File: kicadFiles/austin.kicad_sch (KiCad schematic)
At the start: 482 parts, among them J1 TYPE-C-31-M12_13, J5 Conn_ARM_JTAG_SWD_10, Q1 AO4406AL, SW1 MXSwitch, SW10 MXSwitch, SW100 MXSwitch, SW101 MXSwitch, SW102 MXSwitch, SW103 MXSwitch, SW104 MXSwitch, SW105 MXSwitch, SW106 MXSwitch, SW107 MXSwitch, SW108 MXSwitch, SW109 MXSwitch, SW11 MXSwitch, SW110 MXSwitch, SW111 MXSwitch, SW112 MXSwitch, SW113 MXSwitch, SW114 MXSwitch, SW12 MXSwitch, SW13 MXSwitch, SW14 MXSwitch, SW15 MXSwitch, SW16 MXSwitch, SW17 MXSwitch, SW18 MXSwitch, SW19 MXSwitch, SW2 MXSwitch, SW20 MXSwitch, SW21 MXSwitch, SW22 MXSwitch, SW23 MXSwitch, SW24 MXSwitch, SW25 MXSwitch, SW26 MXSwitch, SW27 MXSwitch, SW28 MXSwitch, SW29 MXSwitch, SW3 MXSwitch, SW30 MXSwitch, SW31 MXSwitch, SW32 MXSwitch, SW33 MXSwitch, SW34 MXSwitch, SW35 MXSwitch, SW36 MXSwitch, SW37 MXSwitch, SW38 MXSwitch, SW39 MXSwitch, SW4 MXSwitch, SW40 MXSwitch, SW41 MXSwitch, SW42 MXSwitch, SW43 MXSwitch, SW44 MXSwitch, SW45 MXSwitch, SW46 MXSwitch, SW47 MXSwitch, SW48 MXSwitch, SW49 MXSwitch, SW5 MXSwitch, SW50 MXSwitch, SW51 MXSwitch, SW52 MXSwitch, SW53 MXSwitch, SW54 MXSwitch, SW55 MXSwitch, SW56 MXSwitch, SW57 MXSwitch, SW58 ANSI LShift, SW59 MXSwitch, SW6 MXSwitch, SW60 MXSwitch, SW61 MXSwitch, SW62 MXSwitch, SW63 MXSwitch, SW64 MXSwitch, SW65 MXSwitch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

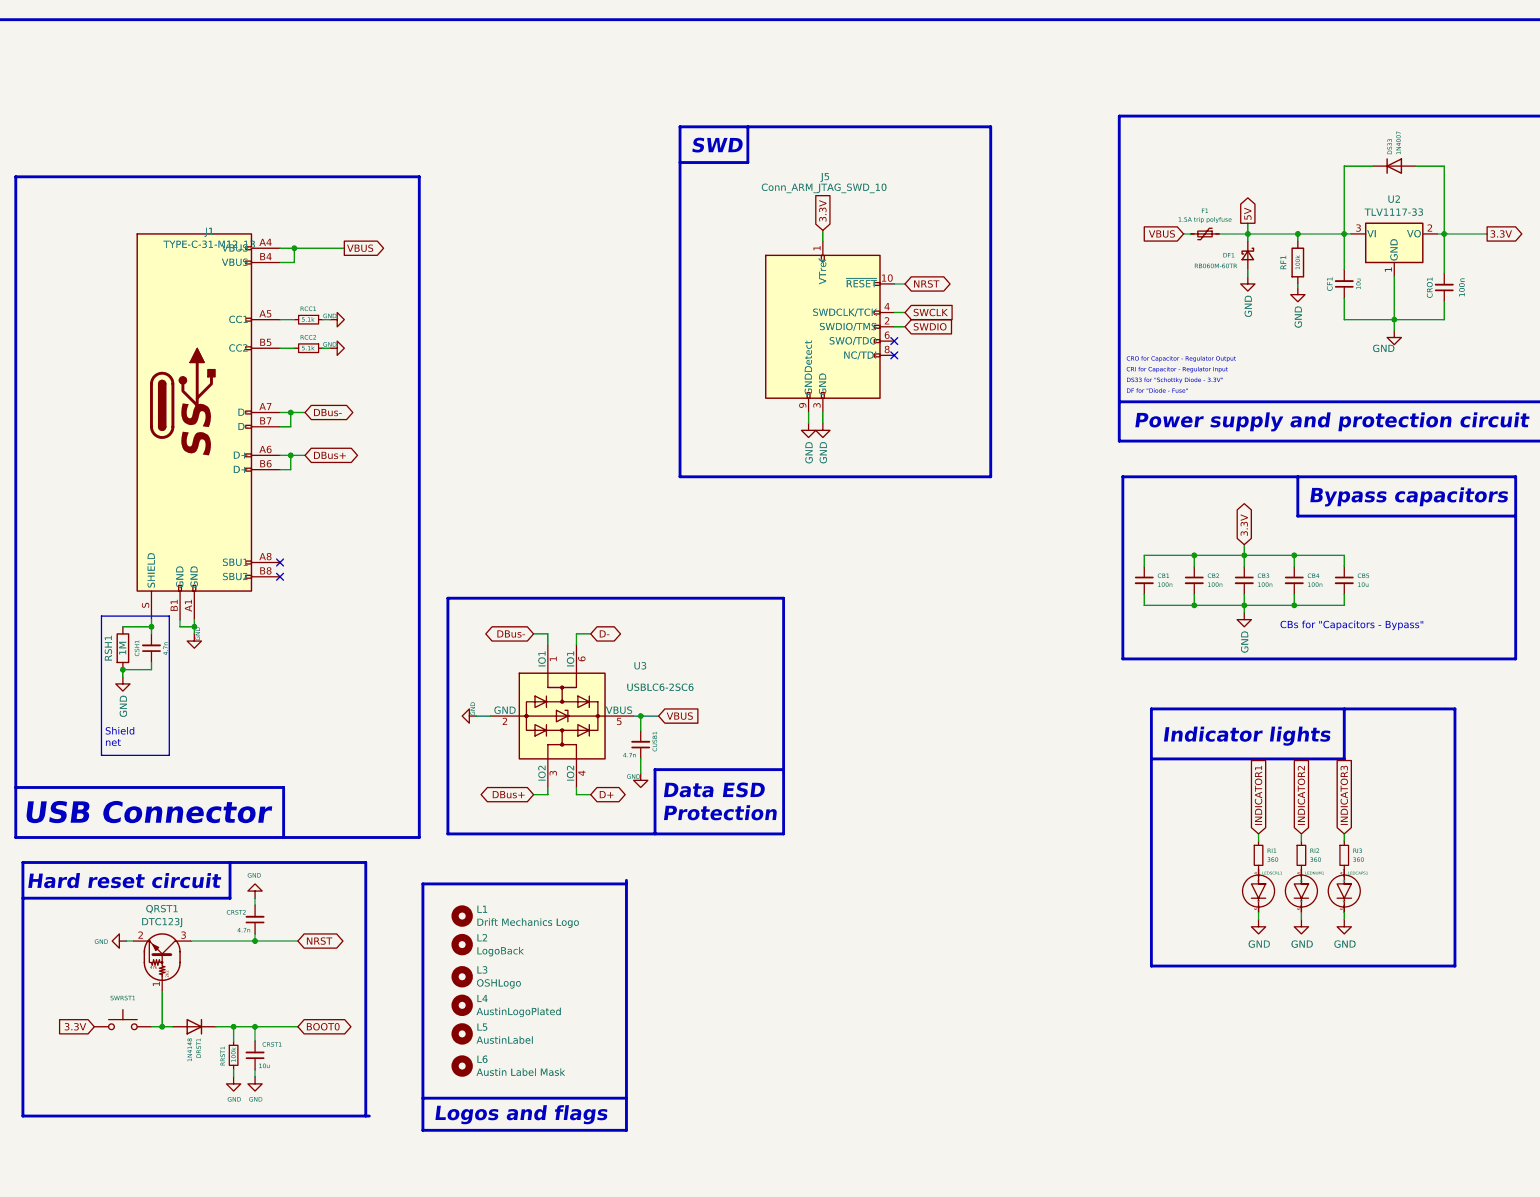
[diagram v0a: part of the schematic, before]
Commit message: Small schematic changes
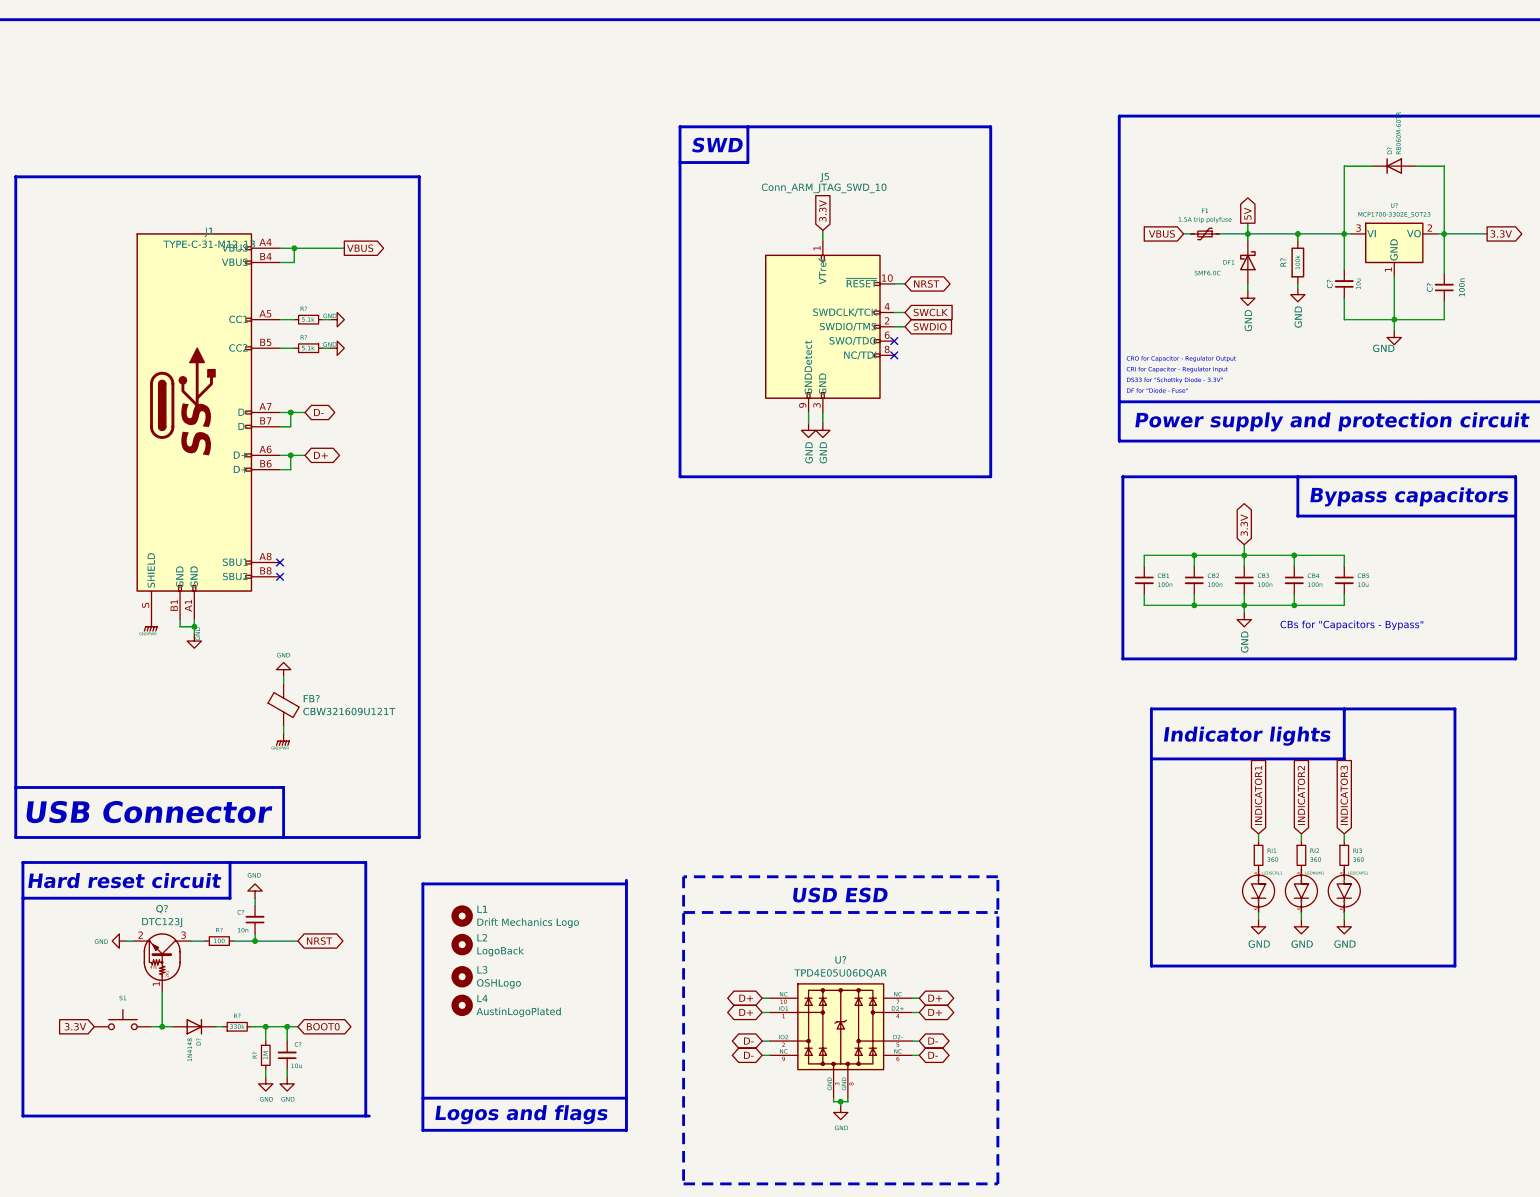
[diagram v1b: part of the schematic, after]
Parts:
- removed CSH1, CUSB1: 4.7n, Capacitor_SMD:C_0805_2012Metric_Pad1.15x1.40mm_HandSolder, symbol Device:C_Small
- removed L5: AustinLabel, austinLogo:austinLabel, symbol Mechanical:MountingHole
- removed L6: Austin Label Mask, austinLogo:austinLabelMask, symbol Mechanical:MountingHole
- removed RSH1: 1M, acheronComponents:R_SMD_1026, symbol Device:R
- removed U2: TLV1117-33, Package_TO_SOT_SMD:SOT-223-3_TabPin2, symbol Regulator_Linear:TLV1117-33
- removed U3: USBLC6-2SC6, acheronComponents:SOT-23-6, symbol austin-rescue:USBLC6-2SC6-Power_Protection
- added FB?: CBW321609U121T, Inductor_SMD:L_1206_3216Metric, symbol Device:Ferrite_Bead
- added R?: 100, acheronComponents:R_SMD_1026, symbol Device:R_Small
- added R?: 330k, acheronComponents:R_SMD_1026, symbol Device:R_Small
- added U?: MCP1700-3302E_SOT23, Package_TO_SOT_SMD:SOT-23, symbol Regulator_Linear:MCP1700-3302E_SOT23
- added U?: TPD4E05U06DQAR, acheron_Components:USON-10_2.5x1.0mm_P0.5mm, symbol acheronSymbols:TPD4E05U06DQAR
- C?: renamed from CRST2; value 4.7n -> 10n
- D?: renamed from DS33; value 1N4007 -> RB060M-60TR
- DF1: value RB060M-60TR -> SMF6.0C; symbol Device:D_Schottky_Small -> Device:D_Schottky
- R?: renamed from RRST1; value 100k -> 1M
- renumbered CF1 to C?, CRO1 to C?, CRST1 to C?, DRST1 to D?, QRST1 to Q?, RCC1 to R?, RCC2 to R?, RF1 to R?, SWRST1 to S1
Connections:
- net DBus+ is gone; now on net D+: J1.A6 (D+), J1.B6 (D+)
- net DBus- is gone; now on net D-: J1.A7 (D-), J1.B7 (D-)
- net 3.3V: now also U?.2 (VO)
- net 5V: now also U?.3 (VI)
- net BOOT0: now also R?.2; no longer D?.1 (K)
- net D+: now also U?.1 (IO1), U?.10 (NC), U?.4 (D2+), U?.7 (NC)
- net D-: now also U?.2 (IO2), U?.5 (D2-), U?.6 (NC), U?.9 (NC)
- net GND: now also FB?.1, U?.1 (GND), U?.3 (GND), U?.8 (GND)
- net NRST: now also R?.2; no longer Q?.3 (C)
- net GNDPWR: now reaches J1.S (SHIELD)
- net GNDPWR: now also FB?.2
- new net: Q?.3 (C), R?.1
- new net: D?.1 (K), R?.1
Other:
- note added: "USD ESD"
- note removed: "Data ESD Protection"
- note removed: "Shield net"
- moved on the sheet: C?, DF1, R?

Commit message: Clean board traces and components, red components, rehaul slkscreen markings
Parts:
- J5: value Conn_ARM_JTAG_SWD_10 -> ARM SWD; footprint Connector_PinHeader_2.54mm:PinHeader_2x05_P2.54mm_Vertical -> acheronConnectors:Conn_ARM_JTAG_SWD_6; symbol Connector:Conn_ARM_JTAG_SWD_10 -> Connector_Generic:Conn_02x03_Odd_Even
- L3: footprint oshLogo:osh-logoExtended -> acheron_Graphics:osh-logo
- R1, R4, R5, R6: renamed from R?; footprint acheronComponents:R_SMD_1026 -> acheronComponents:R_SMD_1206
- R7: renamed from RI1; footprint acheronComponents:R_SMD_1026 -> acheronComponents:R_SMD_1206
- R8: renamed from RI2; footprint acheronComponents:R_SMD_1026 -> acheronComponents:R_SMD_1206
- R9: renamed from RI3; footprint acheronComponents:R_SMD_1026 -> acheronComponents:R_SMD_1206
- RGP1, RGS1, RL1, RL10, RL100, RL101, RL102, RL103, RL104, RL105, RL106, RL107, RL108, RL11, RL12, RL13, RL14, RL15, RL16, RL17, RL18, RL19, RL2, RL20, RL21, RL22, RL23, RL24, RL25, RL26, RL27, RL28, RL29, RL3, RL30, RL31, RL32, RL33, RL34, RL35, RL36, RL37, RL38, RL39, RL4, RL40, RL41, RL42, RL43, RL44, RL45, RL46, RL47, RL48, RL49, RL5, RL50, RL51, RL52, RL53, RL54, RL55, RL56, RL57, RL58, RL6, RL60, RL62, RL63, RL64, RL65, RL66, RL67, RL68, RL69, RL7, RL70, RL71, RL72, RL73, RL74, RL75, RL76, RL77, RL78, RL79, RL8, RL80, RL81, RL82, RL83, RL84, RL85, RL86, RL87, RL88, RL89, RL9, RL90, RL91, RL92, RL93, RL94, RL95, RL96, RL97, RL98, RL99: footprint acheronComponents:R_SMD_1026 -> acheronComponents:R_SMD_1206
- S1: footprint acheronHardware:smdPushBtn -> acheronHardware:K2-1187SQ-A4SW-06
- SW110: footprint austinLogo:MX150 -> acheron_MX:MX150
- SW111: footprint austinLogo:MX700R -> acheron_MX:MX700
- SW113: footprint acheron_MX:MX_ISOEnter -> acheron_MX:MX_ISOEnter_Horizontal
- SW97: footprint austinLogo:MX125 -> acheron_MX:MX125
- SW99: footprint austinLogo:MX625R -> acheron_MX:MX625
- U3: renamed from U?; footprint acheron_Components:USON-10_2.5x1.0mm_P0.5mm -> acheronComponents:USON-10_2.5x1.0mm_P0.5mm
- gave numbers to parts that had none: 11
- renumbered DF1 to D78
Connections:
- net Col1: now also SW60.2 (Row); no longer SW60.1 (Col)
- net Col2: now also SW110.2 (Row); no longer SW110.1 (Col)
- net Col6: now also SW111.2 (Row); no longer SW111.1 (Col)
- net GND: no longer J5.3 (GND), J5.9 (GNDDetect)
- net NRST: no longer J5.10 (~RESET~)
- net at D61.2 (A), SW61.2 (Row): now also SW60.1 (Col); no longer SW60.2 (Row)
- net at D97.2 (A), SW97.2 (Row): now also SW110.1 (Col); no longer SW110.2 (Row)
- net at D99.2 (A), SW99.2 (Row): now also SW111.1 (Col); no longer SW111.2 (Row)
- net SWO: now reaches J5.6 (Pin_6)
- new net nRST: J5.3 (Pin_3)
- no-connect marks 4 -> 2
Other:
- moved on the sheet: SW110, SW111, SW60

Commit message: Revamp copper pours, place and wire MCU
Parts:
- added R10: 100k, acheronComponents:R_SMD_1206, symbol Device:R
- C1: value 10u -> 1u; footprint Capacitor_SMD:C_0805_2012Metric_Pad1.15x1.40mm_HandSolder -> acheronComponents:CP_EIA-3216-10_Kemet-I_Pad1.58x1.35mm_HandSolder; symbol Device:C_Small -> Device:CP_Small
- C2: value 100n -> 1u; footprint Capacitor_SMD:C_0805_2012Metric_Pad1.15x1.40mm_HandSolder -> acheronComponents:CP_EIA-3216-10_Kemet-I_Pad1.58x1.35mm_HandSolder; symbol Device:C_Small -> Device:CP_Small
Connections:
- net 3.3V: now also C2.1, R10.1; no longer C2.2
- net 5V: now also C1.1; no longer C1.2
- net GND: now also C1.2, C2.2, LED1.K, LED10.K, LED100.K, LED101.K, LED102.K, LED103.K, LED104.K, LED105.K, LED106.K, LED107.K, LED108.K, LED109.K, LED11.K, LED110.K, LED111.K, LED112.K, LED113.K, LED114.K, LED115.K, LED12.K, LED13.K, LED14.K, LED15.K, LED16.K, LED17.K, LED18.K, LED19.K, LED2.K, LED20.K, LED21.K, LED22.K, LED23.K, LED24.K, LED25.K, LED26.K, LED27.K, LED28.K, LED29.K, LED3.K, LED30.K, LED31.K, LED32.K, LED33.K, LED34.K, LED35.K, LED36.K, LED37.K, LED38.K, LED39.K, LED4.K, LED40.K, LED41.K, LED42.K, LED43.K, LED44.K, LED45.K, LED46.K, LED47.K, LED48.K, LED49.K, LED5.K, LED50.K, LED51.K, LED52.K, LED53.K, LED54.K, LED55.K, LED56.K, LED57.K, LED58.K, LED59.K, LED6.K, LED60.K, LED61.K, LED62.K, LED63.K, LED64.K, LED65.K, LED66.K, LED67.K, LED68.K, LED69.K, LED7.K, LED70.K, LED71.K, LED72.K, LED73.K, LED74.K, LED75.K, LED76.K, LED77.K, LED78.K, LED79.K, LED8.K, LED80.K, LED81.K, LED82.K, LED83.K, LED84.K, LED85.K, LED86.K, LED87.K, LED88.K, LED89.K, LED9.K, LED90.K, LED91.K, LED92.K, LED93.K, LED94.K, LED95.K, LED96.K, LED97.K, LED98.K, LED99.K, R10.2; no longer C1.1, C2.1, Q1.1, Q1.2, Q1.3, RGP1.1
- removed net LEDK: LED1.K, LED10.K, LED100.K, LED101.K, LED102.K, LED103.K, LED104.K, LED105.K, LED106.K, LED107.K, LED108.K, LED109.K, LED11.K, LED110.K, LED111.K, LED112.K, LED113.K, LED114.K, LED115.K, LED12.K, LED13.K, LED14.K, LED15.K, LED16.K, LED17.K, LED18.K, LED19.K, LED2.K, LED20.K, LED21.K, LED22.K, LED23.K, LED24.K, LED25.K, LED26.K, LED27.K, LED28.K, LED29.K, LED3.K, LED30.K, LED31.K, LED32.K, LED33.K, LED34.K, LED35.K, LED36.K, LED37.K, LED38.K, LED39.K, LED4.K, LED40.K, LED41.K, LED42.K, LED43.K, LED44.K, LED45.K, LED46.K, LED47.K, LED48.K, LED49.K, LED5.K, LED50.K, LED51.K, LED52.K, LED53.K, LED54.K, LED55.K, LED56.K, LED57.K, LED58.K, LED59.K, LED6.K, LED60.K, LED61.K, LED62.K, LED63.K, LED64.K, LED65.K, LED66.K, LED67.K, LED68.K, LED69.K, LED7.K, LED70.K, LED71.K, LED72.K, LED73.K, LED74.K, LED75.K, LED76.K, LED77.K, LED78.K, LED79.K, LED8.K, LED80.K, LED81.K, LED82.K, LED83.K, LED84.K, LED85.K, LED86.K, LED87.K, LED88.K, LED89.K, LED9.K, LED90.K, LED91.K, LED92.K, LED93.K, LED94.K, LED95.K, LED96.K, LED97.K, LED98.K, LED99.K, Q1.5 (D), Q1.6, Q1.7, Q1.8
- new net: Q1.1, Q1.2, Q1.3, RGP1.1
- new net: Q1.5 (D), Q1.6, Q1.7, Q1.8
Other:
- moved on the sheet: Q1, RGP1, RGS1
